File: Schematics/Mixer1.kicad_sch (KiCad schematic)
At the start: 47 parts, among them J46 Conn_01x02, J47 Conn_01x02, J48 Conn_01x02, J49 Conn_01x02, J50 Conn_01x02, J51 Conn_01x02, J52 Conn_01x02, J53 Conn_01x02, J54 Conn_01x03, J55 AudioJack2_Ground, J56 Conn_01x02, U100 LM358, U86 LM358, U98 TL084, U99 TL084

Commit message: Now with dual ESP32 with Midi32 and Disp32.
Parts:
- renumbered C49 to C60, C50 to C61, C51 to C62, C52 to C63, J46 to J52, J47 to J53, J48 to J54, J49 to J55, J50 to J56, J51 to J57, J52 to J58, J53 to J59, J54 to J60, J55 to J61, J56 to J62, R95 to R125, R96 to R126, R97 to R127, R98 to R128, R99 to R129, R100 to R130, R101 to R131, R102 to R132, R103 to R133, R104 to R134, R105 to R135, R106 to R136, R107 to R137, R108 to R138, R109 to R139, R110 to R140, R111 to R141, R112 to R142, R113 to R143, R114 to R144, R115 to R145, R116 to R146, R117 to R147, R118 to R148, R119 to R149, R120 to R150, R121 to R151, RV10 to RV13, U98 to U103, U99 to U104, U100 to U105

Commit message: Disp32 interface working properly.
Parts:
- renumbered J52 to J53, J53 to J54, J54 to J55, J55 to J56, J56 to J57, J57 to J58, J58 to J59, J59 to J60, J60 to J61, J61 to J62, J62 to J63, R125 to R124, R126 to R125, R127 to R126, R128 to R127, R129 to R128, R130 to R129, R131 to R130, R132 to R131, R133 to R132, R134 to R133, R135 to R134, R136 to R135, R137 to R136, R138 to R137, R139 to R138, R140 to R139, R141 to R140, R142 to R141, R143 to R142, R144 to R143, R145 to R144, R146 to R145, R147 to R146, R148 to R147, R149 to R148, R150 to R149, R151 to R150

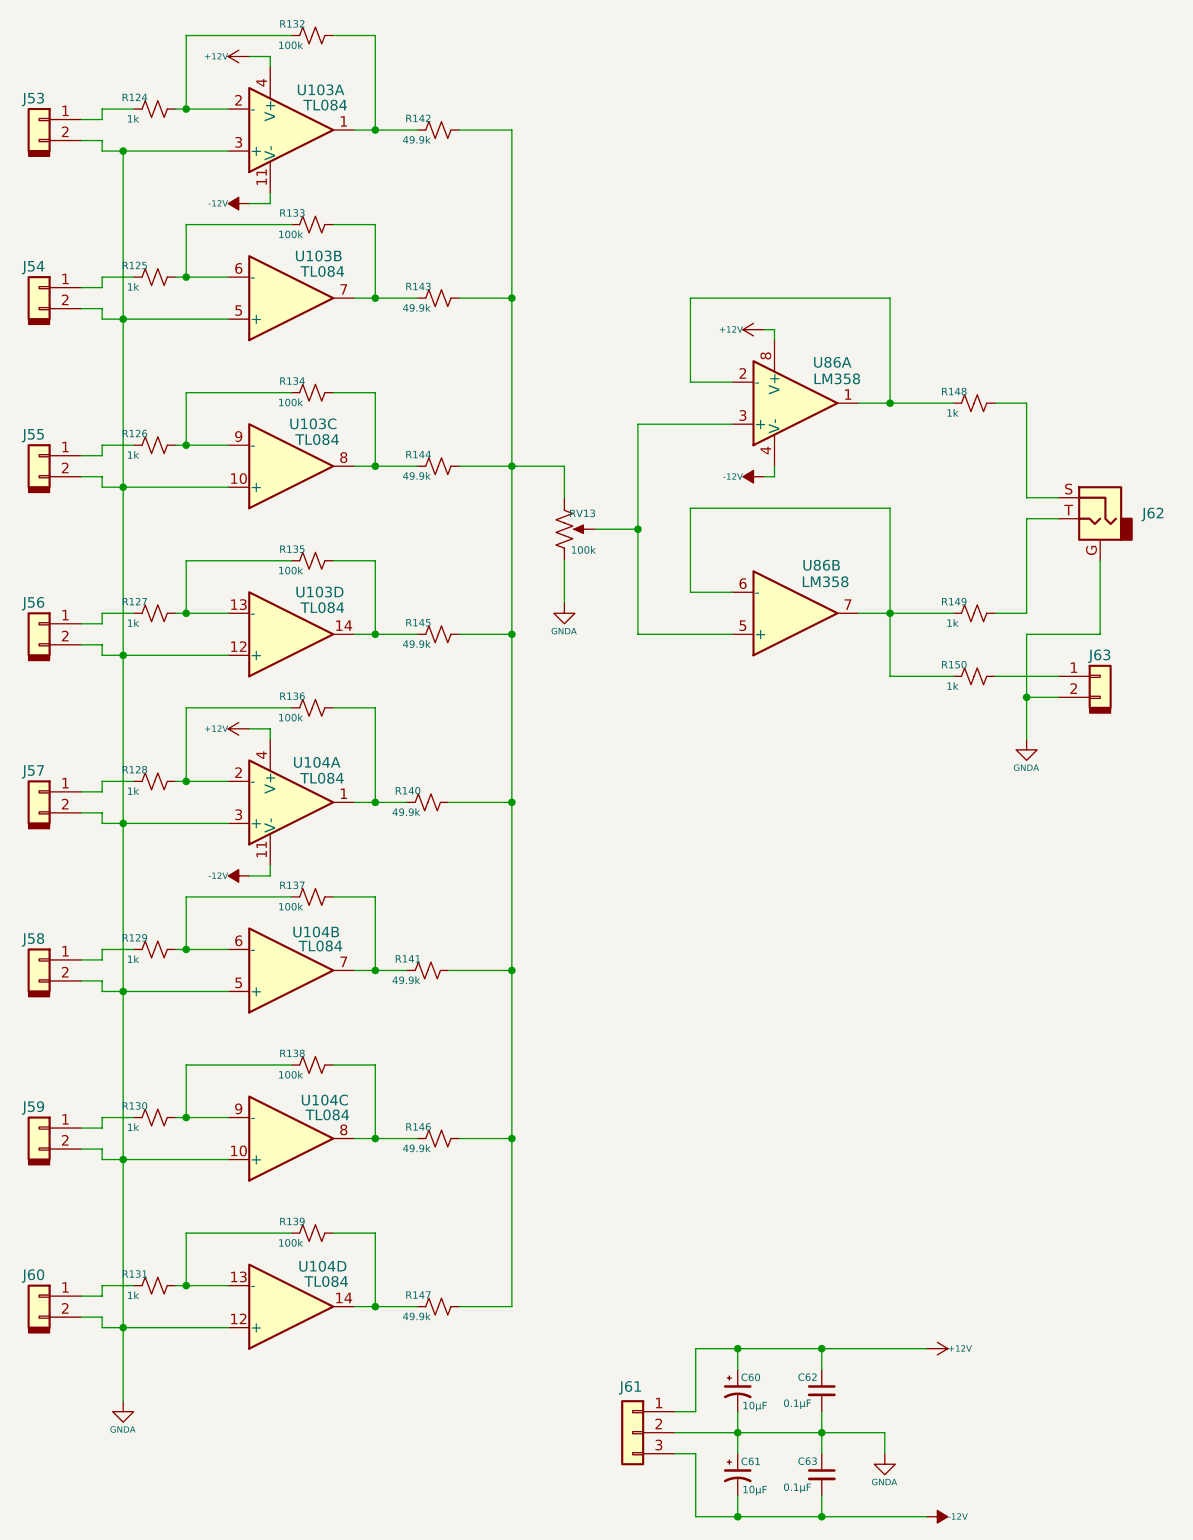
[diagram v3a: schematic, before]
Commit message: adding noise source and variable state filter.
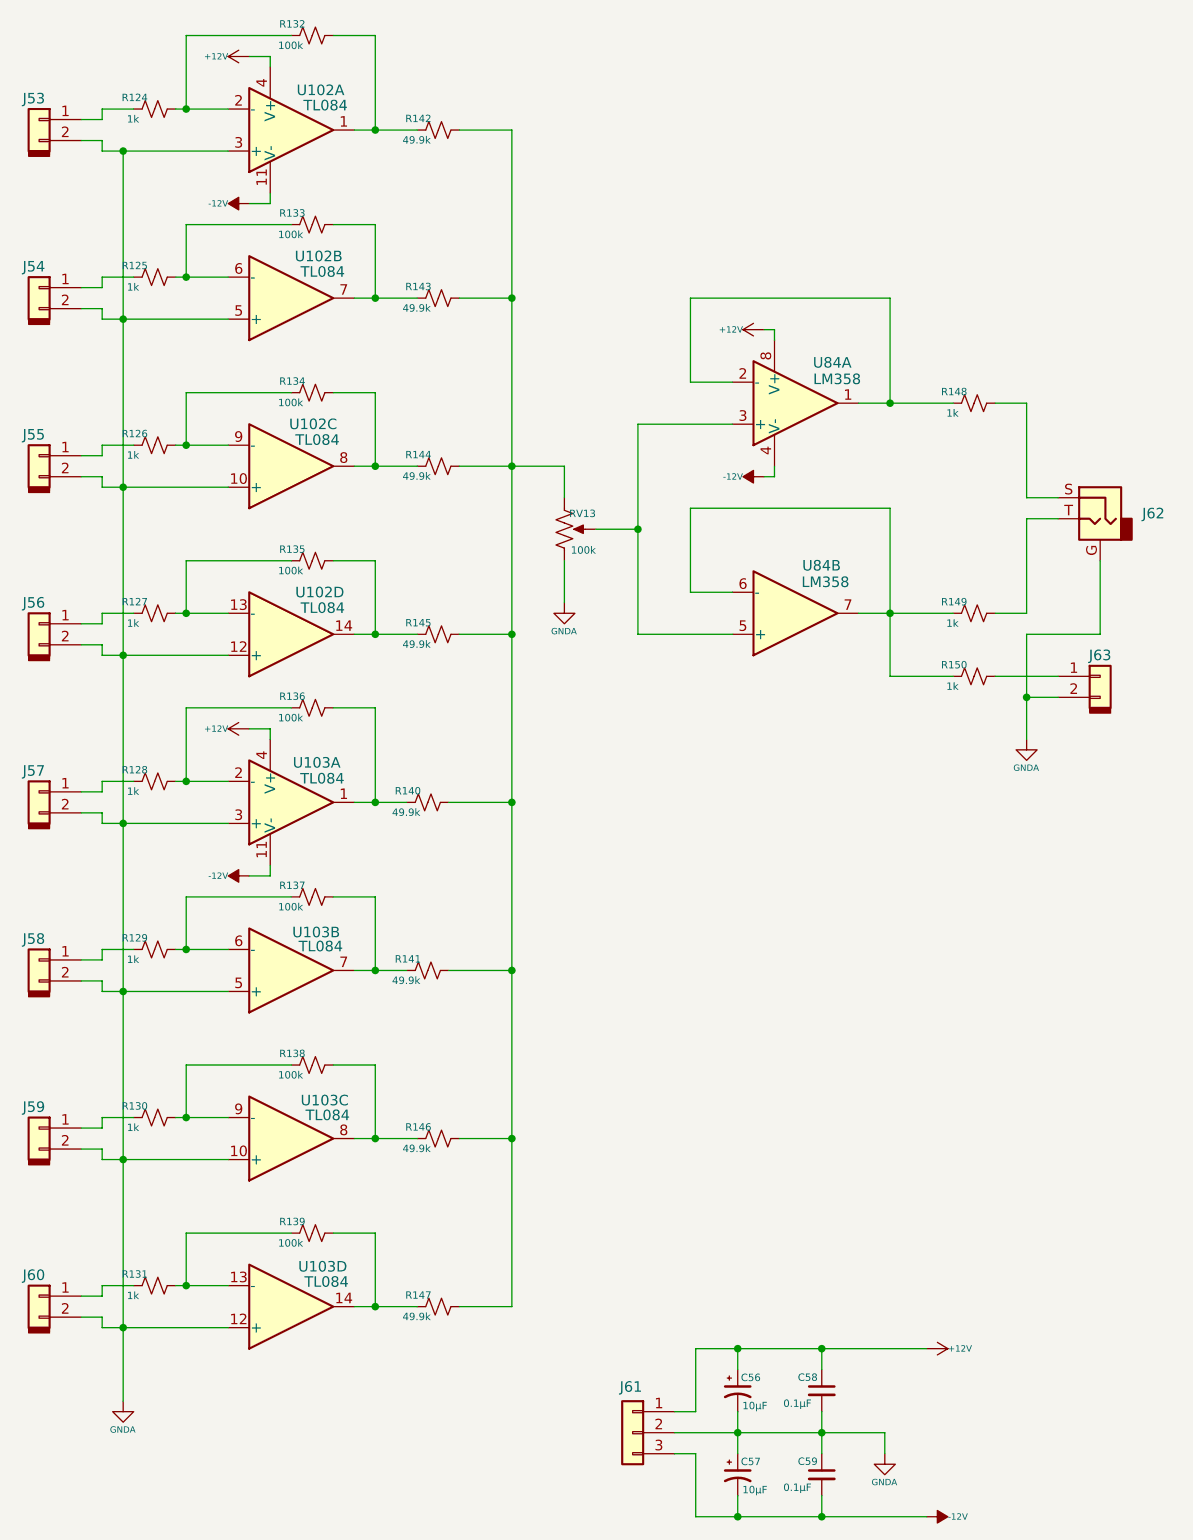
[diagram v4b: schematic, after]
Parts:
- renumbered C60 to C56, C61 to C57, C62 to C58, C63 to C59, U103 to U102, U104 to U103, U105 to U104, U86 to U84

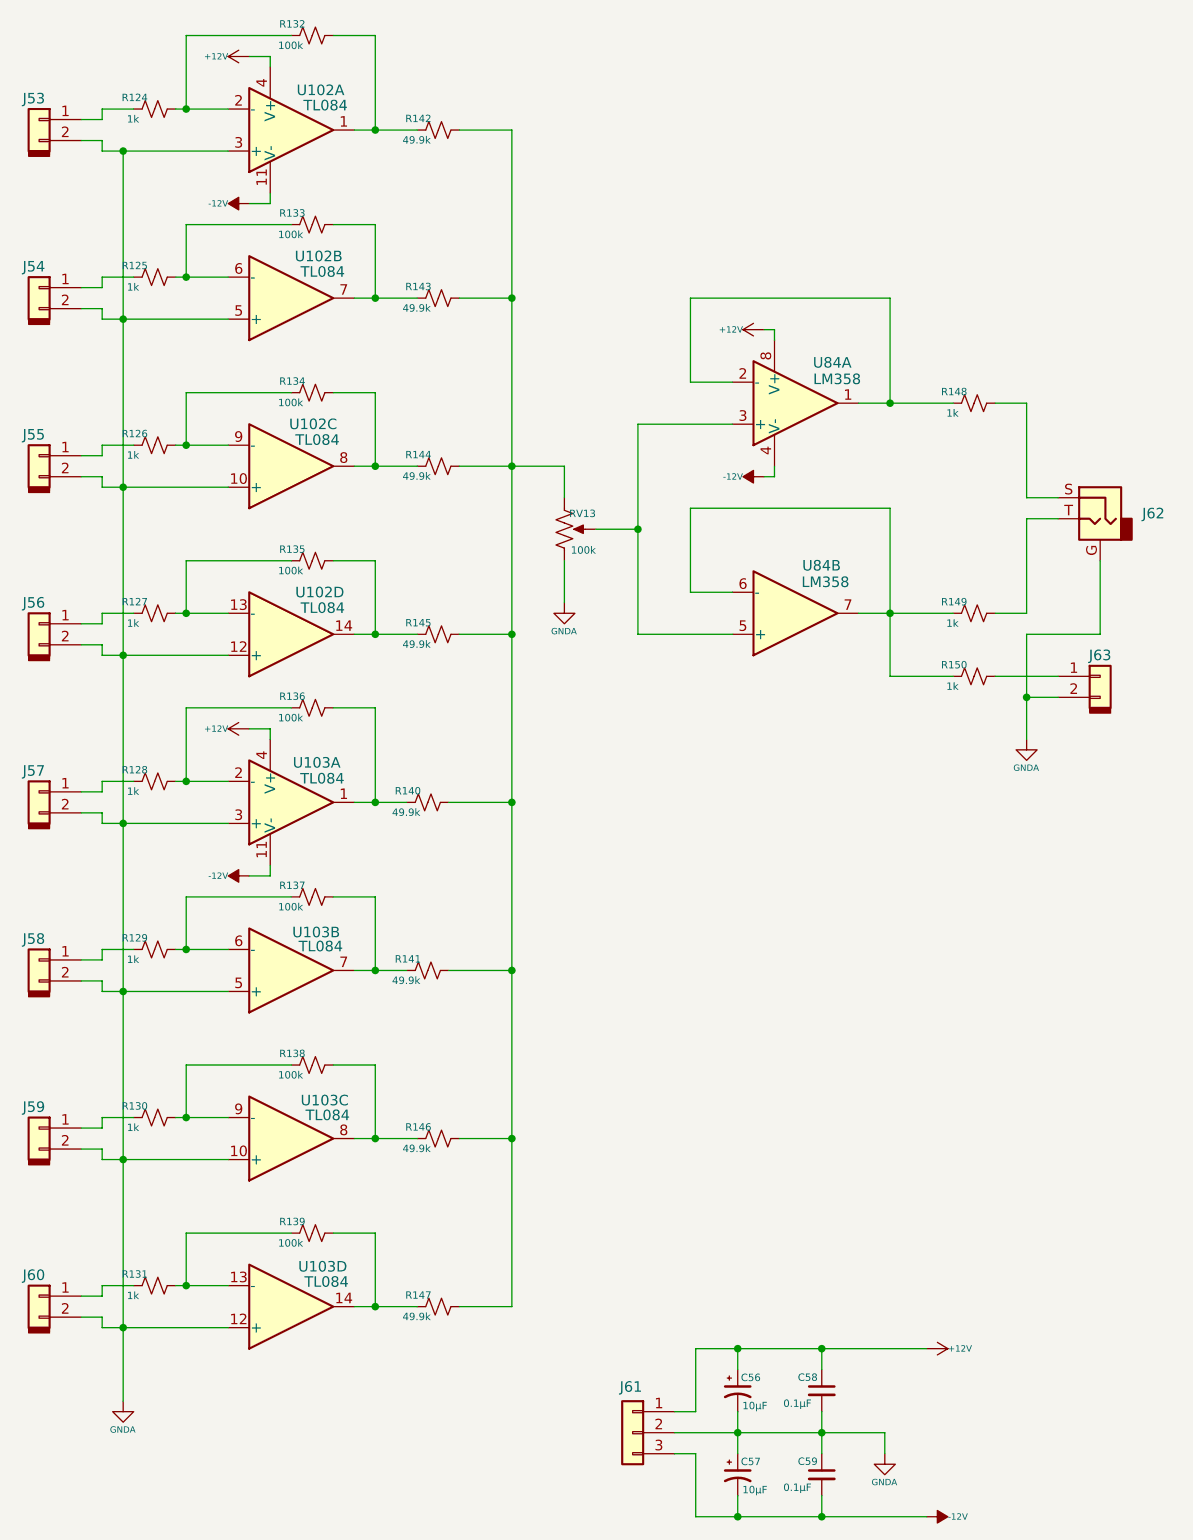
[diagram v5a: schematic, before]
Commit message: Update with noise filter & VCA as well as envelope generator software shell.
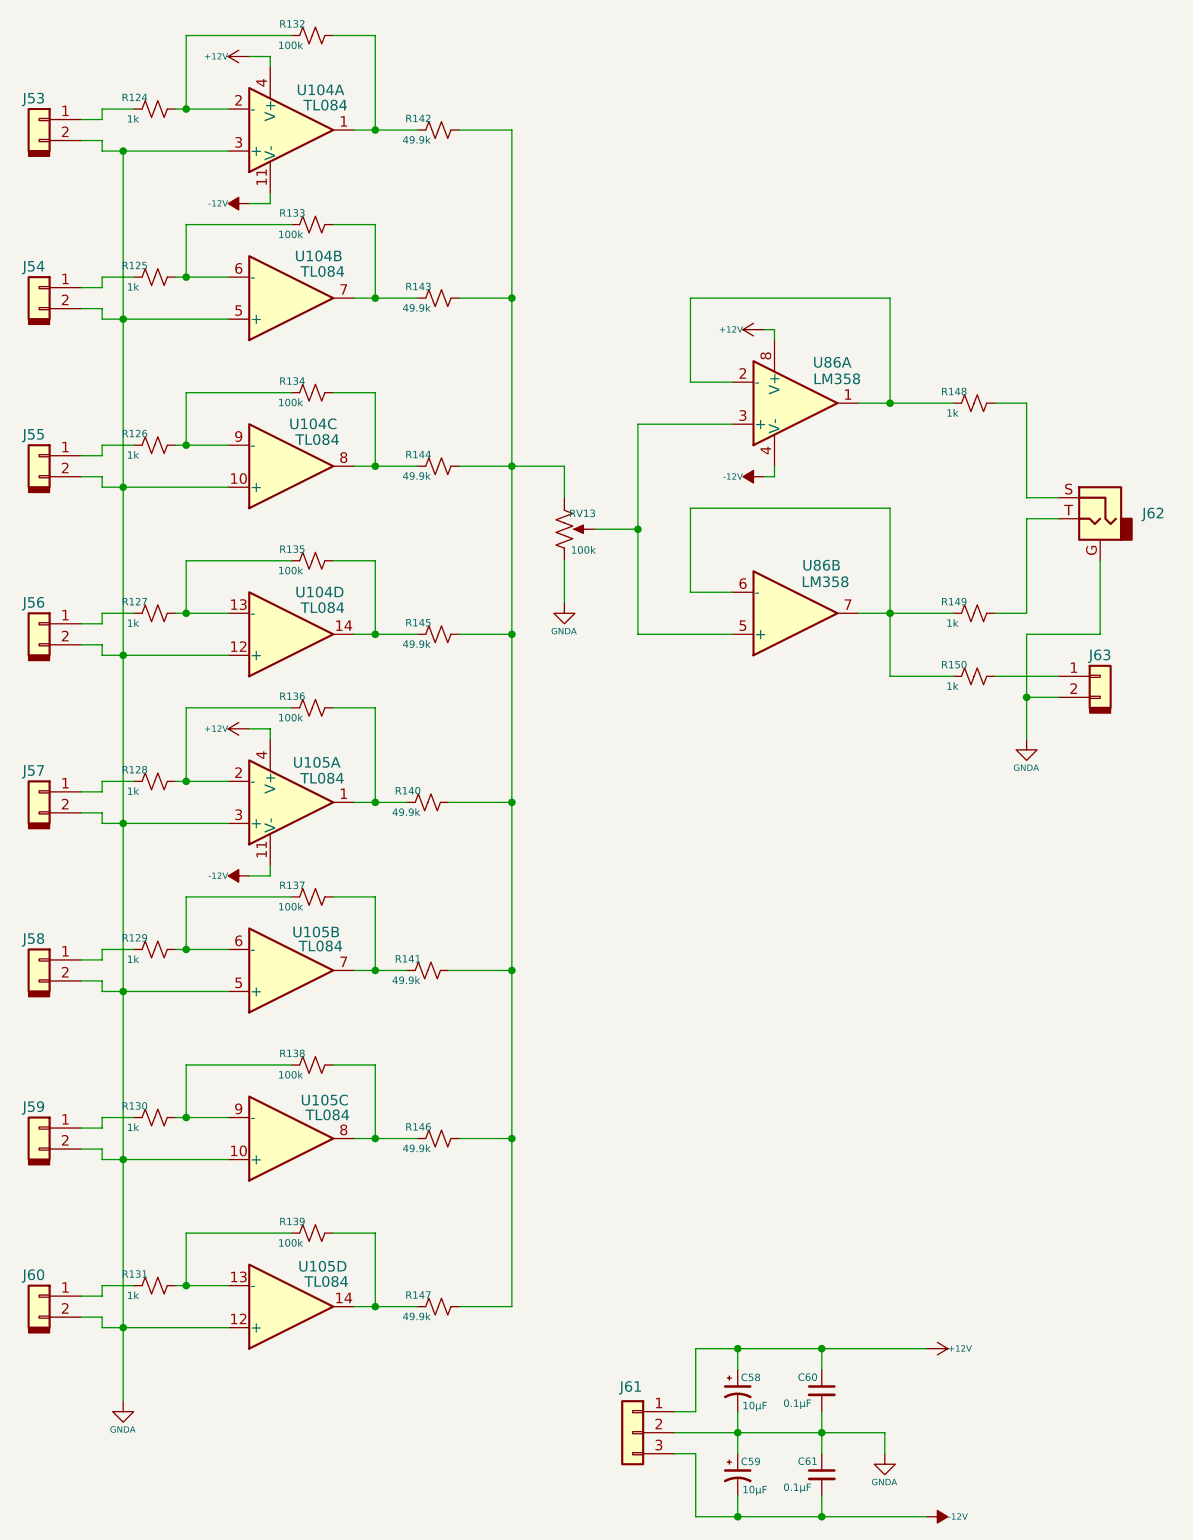
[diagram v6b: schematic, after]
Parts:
- renumbered C56 to C58, C57 to C59, C58 to C60, C59 to C61, U102 to U104, U103 to U105, U104 to U106, U84 to U86
